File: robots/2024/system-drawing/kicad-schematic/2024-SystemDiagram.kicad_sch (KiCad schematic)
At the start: 184 parts

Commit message: Move right side motor PDB connections
Signed-off-by: Scott Berman <sgberman1@gmail.com>
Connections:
- net CATAPULT ALTITUDE PWR: now also PD1.T12; no longer PD1.T14
- net CATAPULT TURRET PWR: now also PD1.T13; no longer PD1.T15
- net RIGHT BACK DRIVE PWR: now also PD1.T15; no longer PD1.T13
- net RIGHT FRONT DRIVE PWR: now also PD1.T14; no longer PD1.T12
- net at POE1. (RJ45S): now also RDO1. (POWER); no longer VRM1. (5V/2A)
- net at RDO1. (POWER): now also ETH1. (POWER); no longer VRM1. (5V/2A)
- net at ETH1. (POWER): now also NX1. (Power), W87.; no longer RDO1. (POWER)
- new net: VRM1. (5V/2A), W118., WG1. (4)
- new net: POE1. (RJ45S), VRM1. (5V/2A)
- new net: RDO1. (POWER), VRM1. (5V/2A)
- new net: CAN1. (USB), W67., WG1. (4)
- new net: IND1. (P), MOT11. (PWR), W114.
- new net: MOT11. (PWR), MOT13. (PWR), W113.
- new net: ETH1. (POWER), NX2. (Power), W88.
- new net: MOT10. (PWR), MOT12. (PWR), W111.
- new net: MOT12. (PWR), MOT13. (PWR), W112.
- new net: VRM2. (5V/2A), W85., WG101. (3)
- new net: IND1. (P), MOT15. (PWR), W115.
- new net: ETH1. (POWER), VRM2. (5V/2A), W84.
- new net: ETH1. (POWER), NX3. (Power), W89.
- new net: PD2. (IN), WG101. (3)
- new net: MOT1. (PWR), MOT2. (PWR), W105.
- new net: MOT3. (PWR), MOT4. (PWR), W107.
- new net: IMU1. (RIO_PWM2), NX3. (Power), W47.
- now unconnected: VRM2. (5V/2A), VRM2. (5V/2A)
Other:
- moved on the sheet: W6, W7
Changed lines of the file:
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@@
   (junction (at 234.95 462.28) (diameter 0) (color 0 0 0 0)
   )
-  (junction (at 487.68 91.44) (diameter 0) (color 255 0 0 1)
-  )
   (junction (at 601.98 462.28) (diameter 0) (color 0 0 0 0)
   )
@@
   (junction (at 138.43 64.77) (diameter 0) (color 255 0 0 1)
   )
+  (junction (at 487.68 99.06) (diameter 0) (color 0 0 0 0)
+  )
   (junction (at 228.6 472.44) (diameter 0) (color 0 0 0 0)
   )
@@
   (junction (at 541.02 439.42) (diameter 0) (color 0 0 0 0)
   )
-  (junction (at 487.68 87.63) (diameter 0) (color 255 0 0 1)
-  )
   (junction (at 240.03 424.18) (diameter 0) (color 0 0 0 0)
   )
@@
   (junction (at 595.63 300.99) (diameter 0) (color 0 0 0 0)
   )
+  (junction (at 487.68 95.25) (diameter 0) (color 0 0 0 0)
+  )
   (junction (at 281.94 492.76) (diameter 0) (color 0 0 0 0)
   )
@@
     (stroke (width 0.508) (type default) (color 132 132 0 1))
   )
-  (wire (pts (xy 487.68 224.79) (xy 452.4022 224.79))
+  (wire (pts (xy 487.68 224.79) (xy 452.12 224.79))
     (stroke (width 0.508) (type default) (color 255 0 0 1))
   )
@@
     (stroke (width 0.508) (type default) (color 255 0 0 1))
   )
-  (wire (pts (xy 457.2 190.5) (xy 457.2 95.25))
-    (stroke (width 0.508) (type default) (color 255 0 0 1))
-  )
   (wire (pts (xy 601.98 289.56) (xy 607.06 289.56))
     (stroke (width 0.254) (type default) (color 255 153 0 1))
@@
     (stroke (width 0.508) (type default) (color 255 0 0 1))
   )
+  (wire (pts (xy 241.3 87.63) (xy 457.2 87.63))
+    (stroke (width 0.508) (type default) (color 255 0 0 1))
+  )
   (wire (pts (xy 579.12 247.65) (xy 579.12 245.11))
     (stroke (width 0) (type default))
@@
     (stroke (width 0.508) (type default) (color 132 132 0 1))
   )
+  (wire (pts (xy 487.68 99.06) (xy 567.69 99.06))
+    (stroke (width 0.508) (type default) (color 255 0 0 1))
+  )
   (wire (pts (xy 106.68 231.14) (xy 87.63 231.14))
     (stroke (width 0.508) (type default) (color 132 132 0 1))
@@
     (stroke (width 0.508) (type default) (color 255 0 0 1))
   )
+  (wire (pts (xy 567.69 91.44) (xy 605.79 91.44))
+    (stroke (width 0.508) (type default) (color 255 0 0 1))
+  )
   (wire (pts (xy 171.45 426.72) (xy 191.77 426.72))
     (stroke (width 0.508) (type default) (color 132 132 0 1))
@@
     (stroke (width 0.254) (type default) (color 194 0 194 1))
   )
+  (wire (pts (xy 567.69 99.06) (xy 567.69 91.44))
+    (stroke (width 0.508) (type default) (color 255 0 0 1))
+  )
   (wire (pts (xy 260.35 184.15) (xy 220.98 184.15))
     (stroke (width 0.254) (type default) (color 194 0 194 1))
@@
     (stroke (width 0) (type default))
   )
-  (wire (pts (xy 487.68 91.44) (xy 605.79 91.44))
-    (stroke (width 0.508) (type default) (color 255 0 0 1))
-  )
   (wire (pts (xy 181.61 149.86) (xy 181.61 143.51))
     (stroke (width 0.508) (type default) (color 255 0 0 1))
@@
     (stroke (width 0.254) (type default) (color 194 0 194 1))
   )
-  (wire (pts (xy 567.69 80.01) (xy 605.79 80.01))
+  (wire (pts (xy 563.88 80.01) (xy 605.79 80.01))
     (stroke (width 0.508) (type default) (color 255 0 0 1))
   )
@@
     (stroke (width 0.254) (type default) (color 194 0 194 1))
   )
-  (wire (pts (xy 452.4022 99.06) (xy 241.3 99.06))
-    (stroke (width 0.508) (type default) (color 255 0 0 1))
-  )
   (wire (pts (xy 289.56 132.08) (xy 289.56 275.59))
     (stroke (width 0.254) (type default) (color 194 0 194 1))
@@
     (stroke (width 0.254) (type default) (color 255 153 0 1))
   )
-  (wire (pts (xy 241.3 87.63) (xy 487.68 87.63))
-    (stroke (width 0.508) (type default) (color 255 0 0 1))
-  )
   (wire (pts (xy 599.44 429.26) (xy 607.06 429.26))
     (stroke (width 0.254) (type default) (color 255 153 0 1))
@@
     (stroke (width 0.508) (type default) (color 255 0 0 1))
   )
-  (wire (pts (xy 457.2 95.25) (xy 241.3 95.25))
-    (stroke (width 0.508) (type default) (color 255 0 0 1))
-  )
   (wire (pts (xy 87.63 245.11) (xy 91.44 245.11))
     (stroke (width 0.254) (type default) (color 255 0 0 1))
@@
     (stroke (width 0.254) (type default) (color 255 153 0 1))
   )
+  (wire (pts (xy 241.3 95.25) (xy 487.68 95.25))
+    (stroke (width 0.508) (type default) (color 255 0 0 1))
+  )
   (wire (pts (xy 119.38 203.2) (xy 96.52 203.2))
     (stroke (width 0.508) (type default) (color 255 0 0 1))
@@
     (stroke (width 0.254) (type default) (color 255 153 0 1))
   )
-  (wire (pts (xy 487.68 87.63) (xy 567.69 87.63))
+  (wire (pts (xy 487.68 95.25) (xy 563.88 95.25))
     (stroke (width 0.508) (type default) (color 255 0 0 1))
   )
@@
     (stroke (width 0.508) (type default) (color 255 0 0 1))
   )
+  (wire (pts (xy 452.12 91.44) (xy 241.3 91.44))
+    (stroke (width 0.508) (type default) (color 255 0 0 1))
+  )
   (wire (pts (xy 421.64 424.18) (xy 421.64 124.46))
     (stroke (width 0.508) (type default) (color 255 0 0 1))
@@
     (stroke (width 0) (type default))
   )
-  (wire (pts (xy 241.3 91.44) (xy 487.68 91.44))
-    (stroke (width 0.508) (type default) (color 255 0 0 1))
-  )
   (wire (pts (xy 165.1 149.86) (xy 181.61 149.86))
     (stroke (width 0.508) (type default) (color 255 0 0 1))
@@
     (stroke (width 0.254) (type default) (color 255 0 0 1))
   )
+  (wire (pts (xy 457.2 87.63) (xy 457.2 190.5))
+    (stroke (width 0.508) (type default) (color 255 0 0 1))
+  )
   (wire (pts (xy 200.66 306.07) (xy 143.51 306.07))
     (stroke (width 0.508) (type default) (color 255 0 0 1))
@@
     (stroke (width 0.254) (type default) (color 0 194 194 1))
   )
-  (wire (pts (xy 567.69 87.63) (xy 567.69 80.01))
+  (wire (pts (xy 563.88 95.25) (xy 563.88 80.01))
     (stroke (width 0.508) (type default) (color 255 0 0 1))
   )
@@
     (stroke (width 0.508) (type default) (color 255 0 0 1))
   )
-  (wire (pts (xy 452.4022 224.79) (xy 452.4022 99.06))
+  (wire (pts (xy 452.12 91.44) (xy 452.12 224.79))
     (stroke (width 0.508) (type default) (color 255 0 0 1))
   )
@@
     (stroke (width 0.508) (type default) (color 255 0 0 1))
   )
+  (wire (pts (xy 241.3 99.06) (xy 487.68 99.06))
+    (stroke (width 0.508) (type default) (color 255 0 0 1))
+  )
   (wire (pts (xy 556.26 46.99) (xy 605.79 46.99))
     (stroke (width 0.508) (type default) (color 255 0 0 1))
@@
     (effects (font (face "FreeSans") (size 1.27 1.27) bold) (justify left bottom))
   )
-  (label "RIGHT BACK DRIVE PWR" (at 242.57 91.44 0) (fields_autoplaced)
+  (label "RIGHT BACK DRIVE PWR" (at 242.57 99.06 0) (fields_autoplaced)
     (effects (font (face "FreeSans") (size 1.27 1.27) bold) (justify left bottom))
   )
@@
     (effects (font (face "FreeSans") (size 1.27 1.27) bold) (justify right bottom))
   )
-  (label "RIGHT FRONT DRIVE PWR" (at 242.57 87.63 0) (fields_autoplaced)
+  (label "RIGHT FRONT DRIVE PWR" (at 242.57 95.25 0) (fields_autoplaced)
     (effects (font (face "FreeSans") (size 1.27 1.27) bold) (justify left bottom))
   )
@@
     (effects (font (face "FreeSans") (size 1.27 1.27) bold) (justify right bottom))
   )
-  (label "CATAPULT TURRET PWR" (at 242.57 99.06 0) (fields_autoplaced)
+  (label "CATAPULT TURRET PWR" (at 242.57 91.44 0) (fields_autoplaced)
     (effects (font (face "FreeSans") (size 1.27 1.27) bold) (justify left bottom))
   )
@@
     (effects (font (face "FreeSans") (size 1.27 1.27) bold) (justify left bottom))
   )
-  (label "CATAPULT ALTITUDE PWR" (at 242.57 95.25 0) (fields_autoplaced)
+  (label "CATAPULT ALTITUDE PWR" (at 242.57 87.63 0) (fields_autoplaced)
     (effects (font (face "FreeSans") (size 1.27 1.27) bold) (justify left bottom))
   )
@@
     )
   )
-  (symbol (lib_id "SystemDiagram:WireTag") (at 487.68 91.44 180) (unit 1)
+  (symbol (lib_id "SystemDiagram:WireTag") (at 487.68 99.06 180) (unit 1)
     (in_bom yes) (on_board yes) (dnp no)
-    (property "Reference" "W7" (at 471.17 90.17 0)
+    (property "Reference" "W7" (at 471.17 97.79 0)
       (effects (font (face "FreeSans") (size 1.524 1.524) bold))
     )
-    (property "Value" "RIGHT BACK DRIVE PWR" (at 487.68 93.98 0)
+    (property "Value" "RIGHT BACK DRIVE PWR" (at 487.68 101.6 0)
       (effects (font (face "FreeSans") (size 1.524 1.524) bold))
     )
-    (property "Footprint" "" (at 487.68 91.44 0)
+    (property "Footprint" "" (at 487.68 99.06 0)
       (effects (font (size 1.27 1.27)) hide)
     )
-    (property "Datasheet" "" (at 487.68 91.44 0)
+    (property "Datasheet" "" (at 487.68 99.06 0)
       (effects (font (size 1.27 1.27)) hide)
     )
@@
     )
   )
-  (symbol (lib_id "SystemDiagram:WireTag") (at 487.68 87.63 0) (unit 1)
+  (symbol (lib_id "SystemDiagram:WireTag") (at 487.68 95.25 0) (unit 1)
     (in_bom yes) (on_board yes) (dnp no)
-    (property "Reference" "W6" (at 471.17 86.36 0)
+    (property "Reference" "W6" (at 471.17 93.98 0)
       (effects (font (face "FreeSans") (size 1.524 1.524) bold))
     )
-    (property "Value" "RIGHT FRONT DRIVE PWR" (at 487.68 85.09 0)
+    (property "Value" "RIGHT FRONT DRIVE PWR" (at 487.68 92.71 0)
       (effects (font (face "FreeSans") (size 1.524 1.524) bold))
     )
-    (property "Footprint" "" (at 487.68 87.63 0)
+    (property "Footprint" "" (at 487.68 95.25 0)
       (effects (font (size 1.27 1.27)) hide)
     )
-    (property "Datasheet" "" (at 487.68 87.63 0)
+    (property "Datasheet" "" (at 487.68 95.25 0)
       (effects (font (size 1.27 1.27)) hide)
     )

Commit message: sat feb 17 system diagram
Signed-off-by: Henry Speiser <henryspeiser@henrys-mbp.mvla.net>
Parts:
- added W120: CATAPULT1 PWR, symbol SystemDiagram:WireTag
- added W121: CATAPULT2 PWR, symbol SystemDiagram:WireTag
- added W122: CATAPULT1 PWM, symbol SystemDiagram:WireTag
- added W123: CAT ENC POT RIO, symbol SystemDiagram:WireTag
- added W124: CATAPULT2 PWM, symbol SystemDiagram:WireTag
- added W125: CAT ALTITUDE ENC POT RIO, symbol SystemDiagram:WireTag
- added W126: CATAPULT ALTITUDE PWR, symbol SystemDiagram:WireTag
- W54: value CAT BEAM BREAK RIO -> TEMP BEAM BREAK RIO
- W63: value CAT BB PWR -> TEMP BB PWR
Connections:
- net CAT ALTITUDE ENC POT RIO: now also W125.
- net CAT ENC POT RIO: now also W123.
- net CATAPULT ALTITUDE PWR: now also PD1.T4, W126.; no longer PD1.T12
- net CATAPULT1 PWM: now also W122.
- net CATAPULT1 PWR: now also W120.
- net CATAPULT2 PWM: now also W124.
- net CATAPULT2 PWR: now also W121.
- net CLIMBER PWR: now also PD1.T11; no longer PD1.T8
- net INTAKE ROLLER PWR: now also PD1.T12; no longer PD1.T4
- net NOTE RETENTION PWR: now also PD1.T6; no longer PD1.T10
- net PDF POWER: now also PD1.T8; no longer PD1.T11
- net TRANSFER ROLLER PWR: now also PD1.T10; no longer PD1.T6
- net at POE1. (RJ45S): now also RDO1. (POWER); no longer VRM1. (5V/2A)
- net at RDO1. (POWER): now also ETH1. (POWER); no longer VRM1. (5V/2A)
- net at ETH1. (POWER): now also NX1. (Power), W87.; no longer RDO1. (POWER)
- net CAT BEAM BREAK renamed TEMP BEAM BREAK
- new net: VRM1. (5V/2A), W118., WG1. (4)
- new net: POE1. (RJ45S), VRM1. (5V/2A)
- new net: RDO1. (POWER), VRM1. (5V/2A)
- new net: CAN1. (USB), W67., WG1. (4)
- new net: IND1. (P), MOT11. (PWR), W114.
- new net: MOT11. (PWR), MOT13. (PWR), W113.
- new net: ETH1. (POWER), NX2. (Power), W88.
- new net: MOT10. (PWR), MOT12. (PWR), W111.
- new net: MOT12. (PWR), MOT13. (PWR), W112.
- new net: VRM2. (5V/2A), W85., WG101. (3)
- new net: IND1. (P), MOT15. (PWR), W115.
- new net: ETH1. (POWER), VRM2. (5V/2A), W84.
- new net: ETH1. (POWER), NX3. (Power), W89.
- new net: PD2. (IN), WG101. (3)
- new net: MOT1. (PWR), MOT2. (PWR), W105.
- new net: MOT3. (PWR), MOT4. (PWR), W107.
- new net: IMU1. (RIO_PWM2), NX3. (Power), W47.
- now unconnected: VRM2. (5V/2A), VRM2. (5V/2A)
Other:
- moved on the sheet: W50, W51

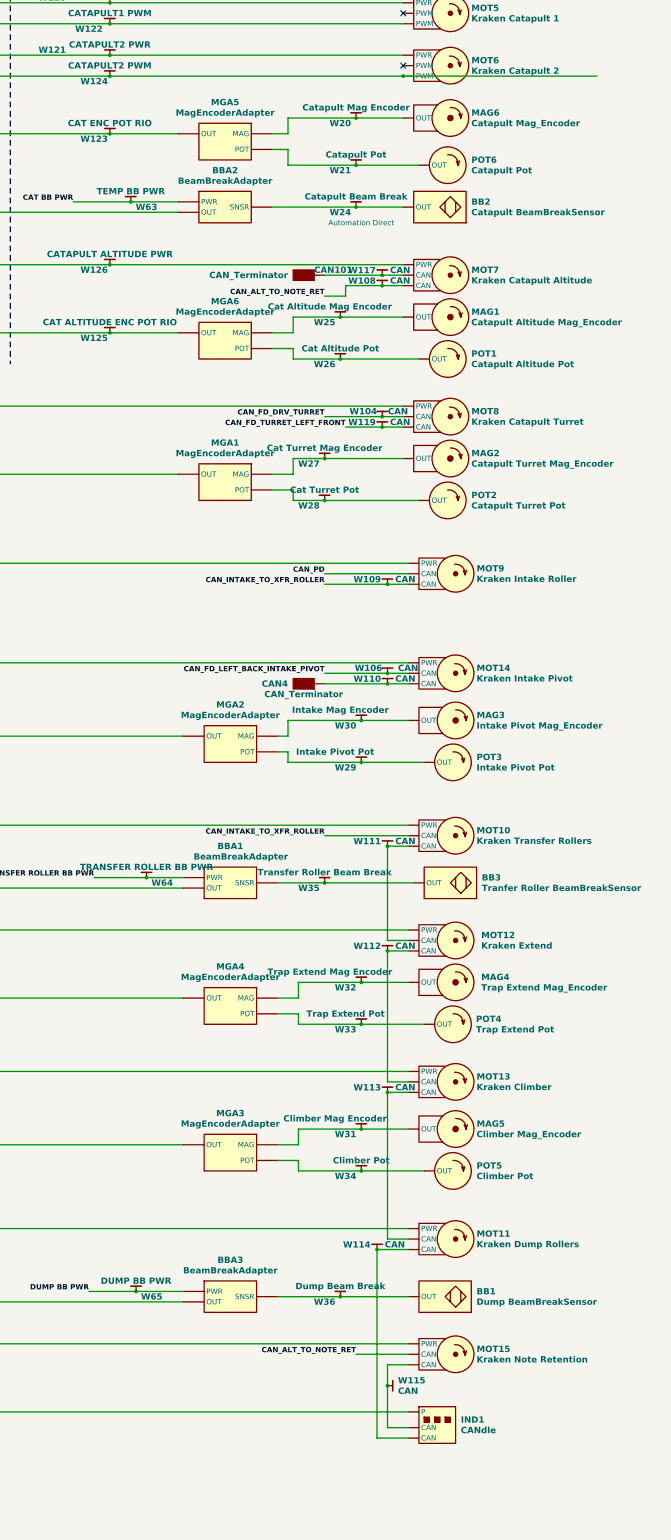
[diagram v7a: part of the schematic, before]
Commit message: Update system diagram can bus
Signed-off-by: Scott Berman <sgberman1@gmail.com>
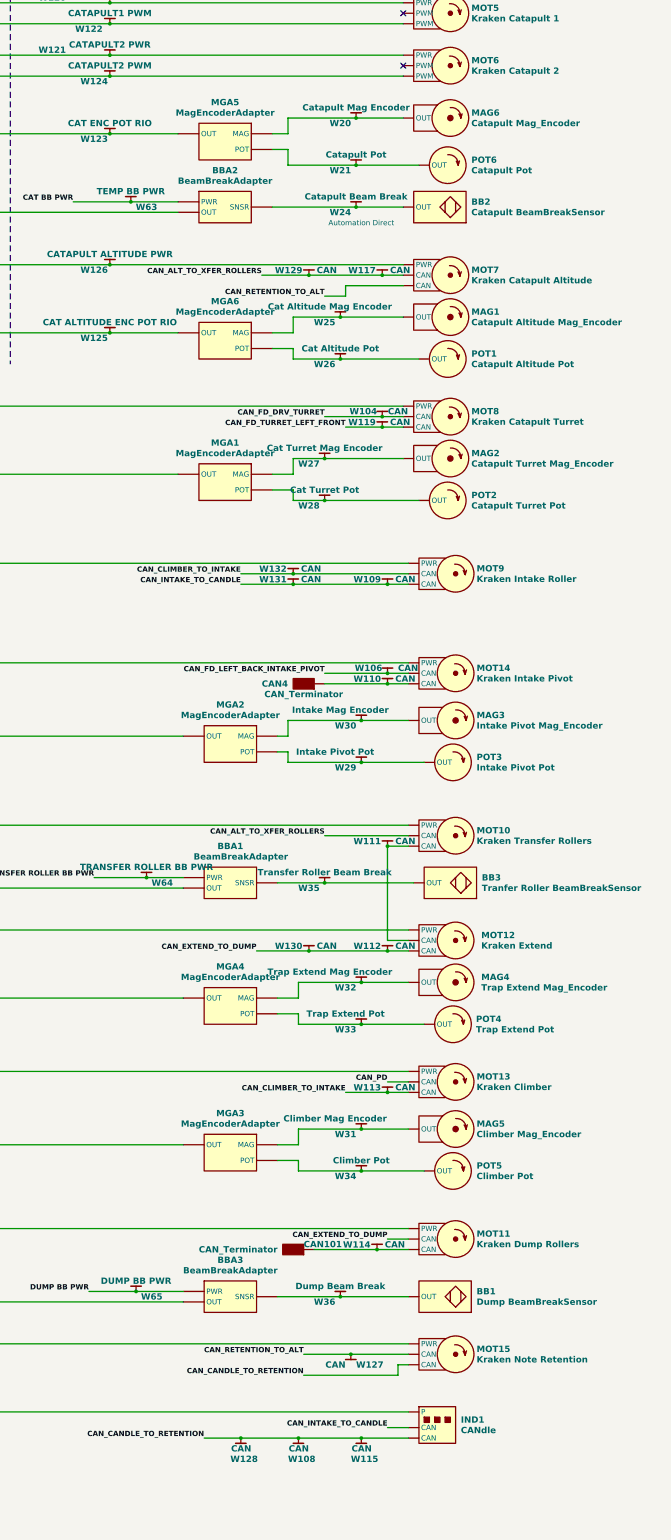
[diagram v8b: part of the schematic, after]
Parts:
- added W127, W128, W129, W130, W131, W132: CAN, symbol SystemDiagram:WireTag
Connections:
- net CAN_PD: now also MOT13. (PWR); no longer MOT9. (PWR)
- net at POE1. (RJ45S): now also RDO1. (POWER); no longer VRM1. (5V/2A)
- net at RDO1. (POWER): now also ETH1. (POWER); no longer VRM1. (5V/2A)
- net at ETH1. (POWER): now also NX1. (Power), W87.; no longer RDO1. (POWER)
- removed net CAN_ALT_TO_NOTE_RET: MOT15. (PWR), MOT7. (PWR), W108.
- removed net CAN_INTAKE_TO_XFR_ROLLER: MOT10. (PWR), MOT9. (PWR), W109.
- new net: VRM1. (5V/2A), W118., WG1. (4)
- new net: POE1. (RJ45S), VRM1. (5V/2A)
- new net: RDO1. (POWER), VRM1. (5V/2A)
- new net: CAN101., MOT11. (PWR), W114.
- new net: CAN1. (USB), W67., WG1. (4)
- new net: ETH1. (POWER), NX2. (Power), W88.
- new net: MOT10. (PWR), MOT12. (PWR), W111.
- new net: VRM2. (5V/2A), W85., WG101. (3)
- new net: ETH1. (POWER), VRM2. (5V/2A), W84.
- new net: ETH1. (POWER), NX3. (Power), W89.
- new net: PD2. (IN), WG101. (3)
- new net: MOT1. (PWR), MOT2. (PWR), W105.
- new net: MOT3. (PWR), MOT4. (PWR), W107.
- new net: IMU1. (RIO_PWM2), NX3. (Power), W47.
- new net CAN_ALT_TO_XFER_ROLLERS: MOT10. (PWR), MOT7. (PWR), W117., W129.
- new net CAN_CANDLE_TO_RETENTION: IND1. (P), MOT15. (PWR), W108., W115., W128.
- new net CAN_CLIMBER_TO_INTAKE: MOT13. (PWR), MOT9. (PWR), W113., W132.
- new net CAN_EXTEND_TO_DUMP: MOT11. (PWR), MOT12. (PWR), W112., W130.
- new net CAN_INTAKE_TO_CANDLE: IND1. (P), MOT9. (PWR), W109., W131.
- new net CAN_RETENTION_TO_ALT: MOT15. (PWR), MOT7. (PWR), W127.
- now unconnected: VRM2. (5V/2A), VRM2. (5V/2A)
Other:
- moved on the sheet: W115
